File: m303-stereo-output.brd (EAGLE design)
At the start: 100 x 50 mm, 76 parts, among them U1 SCREW-M2X8, U2 SCREW-M2X8, U3 NUT-M2-SELFLOCK, U4 NUT-M2-SELFLOCK, U5 FX2-20S-1.27DS, U6 ERM1-5MM

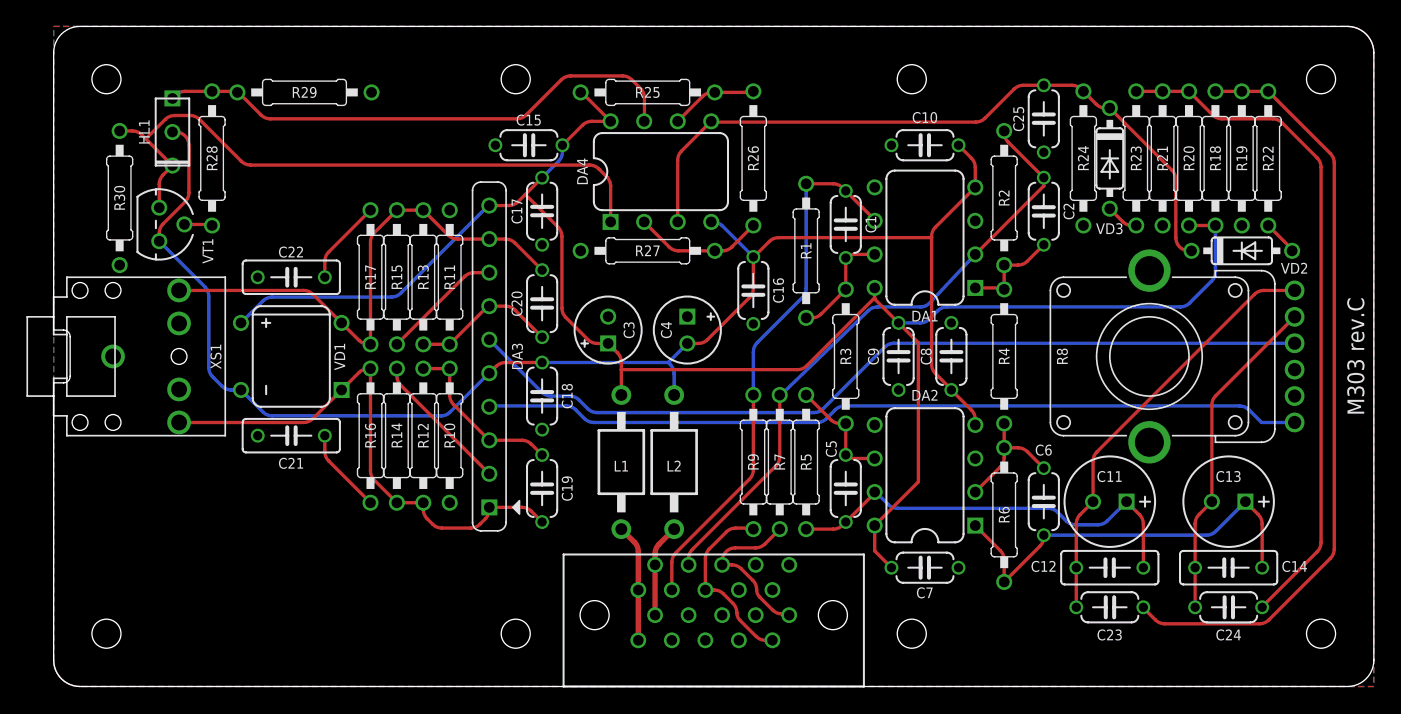
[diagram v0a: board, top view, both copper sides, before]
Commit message: M303 rev.D: Updated signal indicator
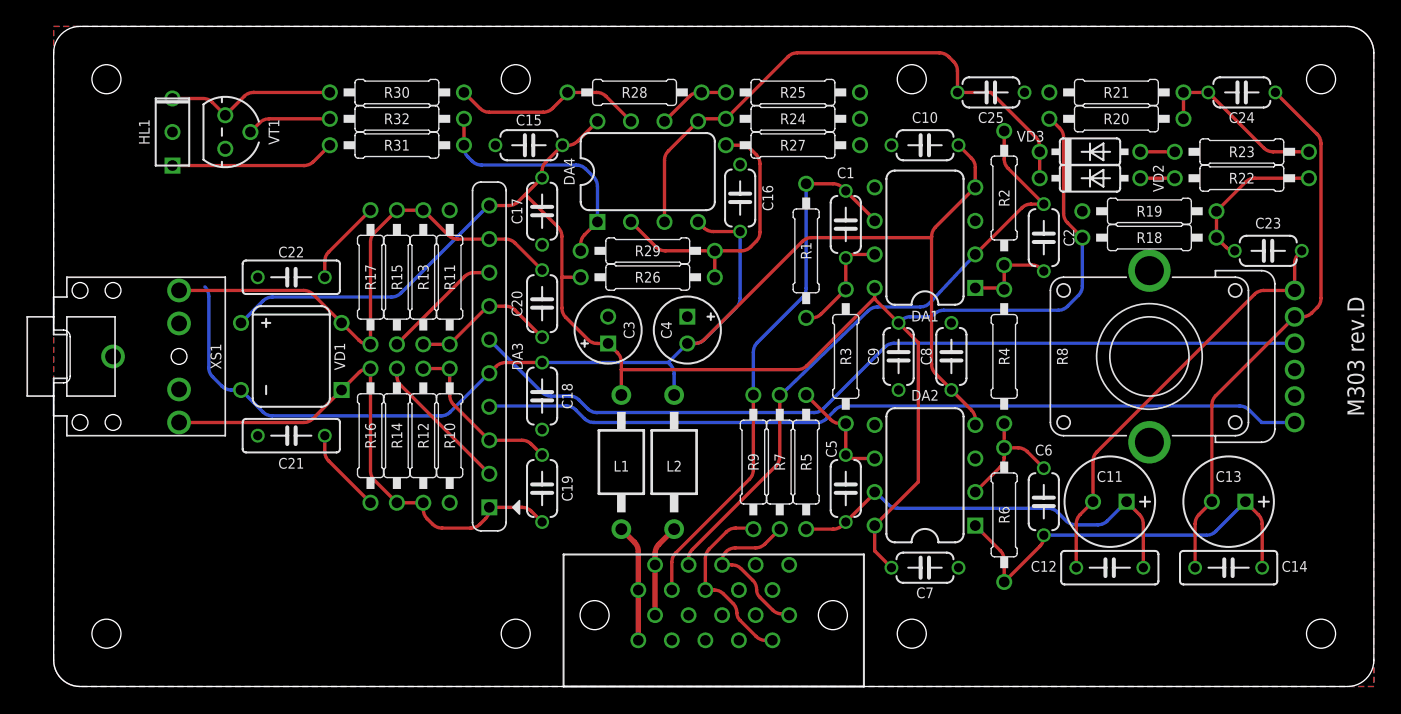
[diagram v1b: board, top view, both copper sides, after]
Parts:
- added R31: 1K(TH), resistors:R-0207/10
- added R32: 300K(TH), resistors:R-0207/10
- DA4: value LM2903N -> TL072IP; device ic-fairchild:DIP-8 -> ic-ti:DIP-8
- HL1: value RED/BLUE(2MMX5MM,CC) -> RED/GREEN(2MMX5MM,CC)
- PCB1: value M303 rev.C -> M303 rev.D
- R18, R20: value 10M(TH) -> 1M(TH)
- R19, R21: value 100K(TH) -> 33K(TH)
- R25: value 22K(TH) -> 10K(TH)
- R26: value 4K7(TH) -> 470K(TH)
- R27: value 100R(TH) -> 15K(TH)
- R28: value 10K(TH) -> 100K(TH)
- R29: value 2K2(TH) -> 100K(TH)
- R30: value 1K8(TH) -> 1K(TH)
- moved U6 42.4 mm to (7.00, -151.0)
- moved C24 39.0 mm to (90.0, 45.0), turned to 180 degrees
- moved R28 32.4 mm to (44.0, 45.0), turned to 180 degrees
- moved C23 29.5 mm to (92.0, 33.0), turned to 180 degrees
- moved R29 28.6 mm to (45.0, 33.0), turned to 180 degrees
- moved R30 22.5 mm to (26.0, 45.0), turned to 180 degrees
- moved R24 22.2 mm to (56.0, 43.0), turned to 180 degrees
- moved R27 13.6 mm to (56.0, 41.0), turned to 180 degrees
- moved VD2 12.7 mm to (78.5, 38.5)
- moved R26 12.0 mm to (45.0, 31.0), turned to 0 degrees
- moved R25 11.0 mm to (56.0, 45.0)
- moved VT1 8.60 mm to (13.0, 42.0)
- moved R19 8.06 mm to (83.0, 36.0), turned to 0 degrees
- moved R23 8.02 mm to (90.0, 40.5), turned to 180 degrees
- moved R18 7.81 mm to (83.0, 34.0), turned to 180 degrees
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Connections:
- removed net N$23 (its old number): DA4.2, R26.1, R27.2
- removed net N$25: DA4.1, HL1.A2, R30.1, VT1.1
- removed net N$47: DA4.6, R25.1, R26.2
- removed net N$48: DA4.7, HL1.A1, R28.2, R29.1
- removed net N$49: R28.1, VT1.2
- new net N$13: DA4.6, R25.2, R28.1
- new net N$17: DA4.7, R28.2, R30.1
- new net N$29: HL1.A2, R30.2, VT1.1
- new net N$30: DA4.2, R26.2, R27.2, R29.1
- new net N$31: DA4.1, R29.2, R31.1, R32.1
- new net N$32: R32.2, VT1.2
- new net N$33: HL1.A1, R31.2
- net +15V: now also R26.1; no longer R25.2
- net -15V: no longer HL1.K, VT1.3
- net GND: now also HL1.K, R25.1, VT1.3; no longer R29.2, R30.2
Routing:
- net N$25: track 49.4 -> 0.00 mm
- net N$20: track 58.1 -> 11.7 mm
- net N$48: track 40.5 -> 0.00 mm
- net N$2: track 51.6 -> 13.3 mm
- net N$30: track 0.00 -> 21.8 mm
- net N$31: track 0.00 -> 19.1 mm
- net N$10: track 25.0 -> 41.7 mm
- net N$17: track 0.00 -> 14.7 mm
- net N$29: track 0.00 -> 13.0 mm
- net N$33: track 0.00 -> 12.5 mm
- net N$4: track 53.9 -> 43.2 mm
- net N$23 (its old number): track 9.85 -> 0.00 mm
- net N$47: track 6.61 -> 0.00 mm
- net -15V: track 115.0 -> 108.7 mm
- net N$32: track 0.00 -> 6.37 mm
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
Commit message: M303d Resistor Value Update
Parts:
- R32: value 300K(TH) -> 330K(TH)
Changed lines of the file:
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@@
 <element name="R27" library="resistors" package="R-0207/10" value="15K(TH)" x="56" y="41" rot="R180"/>
 <element name="R26" library="resistors" package="R-0207/10" value="470K(TH)" x="45" y="31"/>
-<element name="R32" library="resistors" package="R-0207/10" value="300K(TH)" x="26" y="43" rot="R180"/>
+<element name="R32" library="resistors" package="R-0207/10" value="330K(TH)" x="26" y="43" rot="R180"/>
 <element name="R31" library="resistors" package="R-0207/10" value="1K(TH)" x="26" y="41" rot="R180">
 <attribute name="MOUSER" value="71-RN55D-F-1.0K" x="46" y="81" size="1.778" layer="27" rot="R180" display="off"/>
